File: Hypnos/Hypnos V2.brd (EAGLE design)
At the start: 25.5 x 51 mm, 25 parts

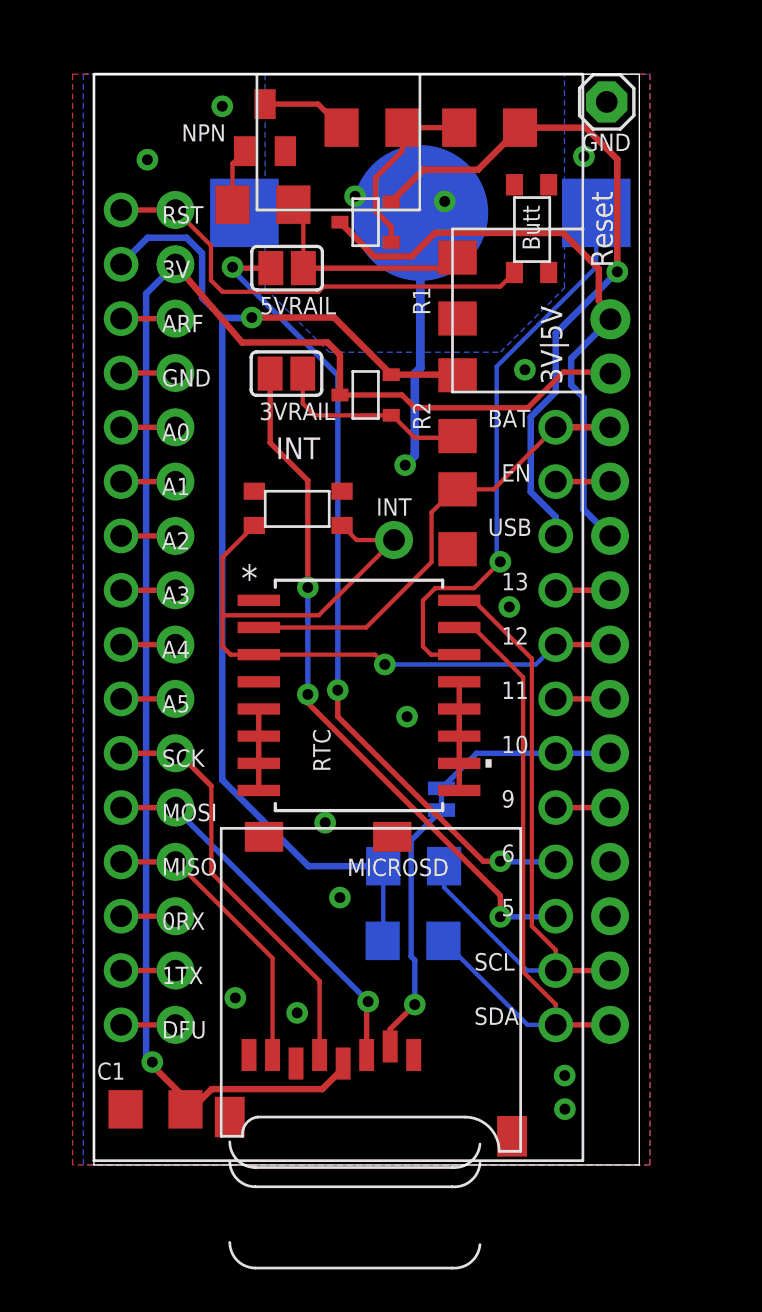
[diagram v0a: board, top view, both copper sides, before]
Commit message: Testing for Version V2
Update from Version 1:
* 2 LEDs with current limiting resistors
* RTC is now powered from 3V3 instead of Vbat (using power from Vbat turns on Feather Battery Charger LED)
* Pull up resistor for SD chip select just like adalogger
* Rounded PCB corner
* Move the reset button to the middle of the board - mechanically more stable
* Add solder jumper for RTC-INT, normally connected

These LED has very high efficiency and only draw around 2mA instead of 20mA
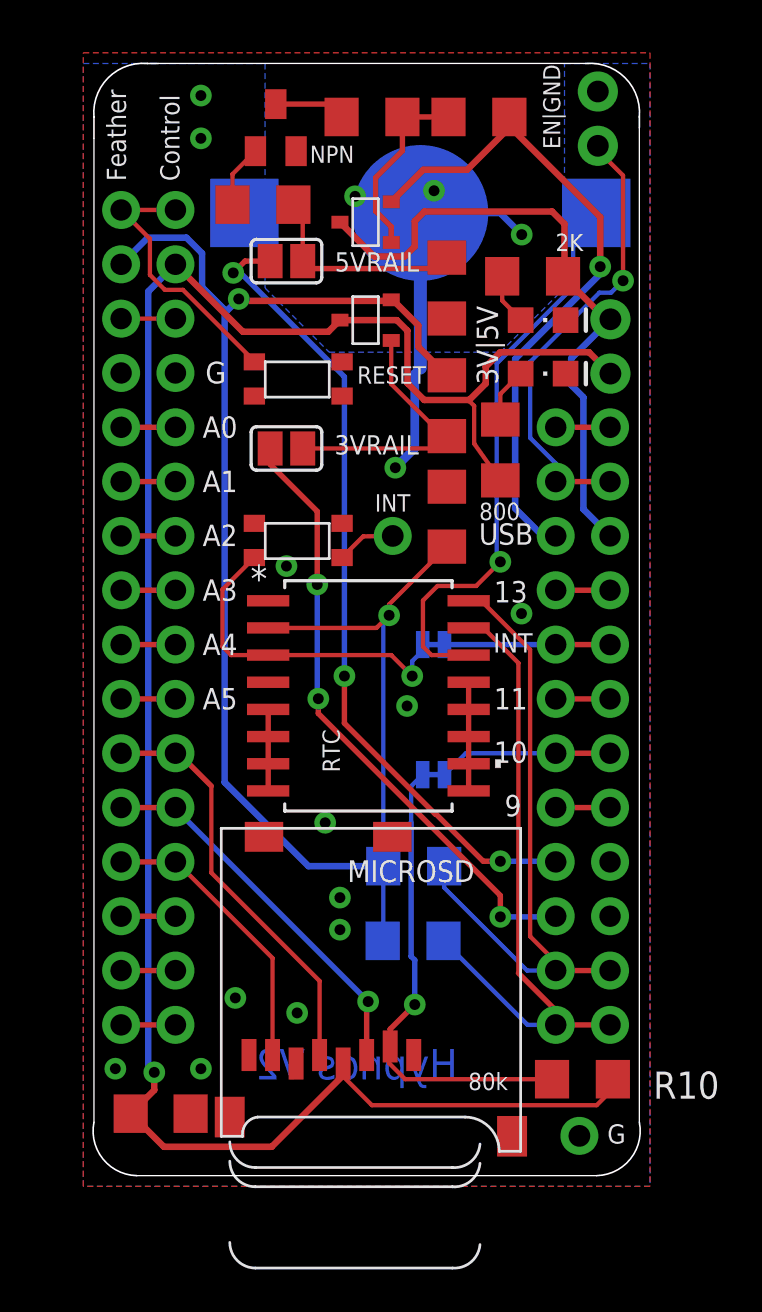
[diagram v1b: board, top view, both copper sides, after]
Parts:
- removed FEATHER: BLUEFRUIT_M0, bluefruit_m0:BLUEFRUIT_MO
- removed GND: (no value), adafruitmodified:1X01
- added EN|GND: (no value), SparkFun-Connectors:1X02_NO_SILK
- added JP1: (no value), adafruit:1X01-CLEANBIG
- added LED1, LED2: RED, adafruit:CHIPLED_0805
- added MS2: FEATHERWING, adafruit:FEATHERWING
- added R10: 80k, adafruit:R1206
- added R8: 2k, adafruit:R1206
- added R9: 820, adafruit:R1206
- added RTC_INT: (no value), SparkFun-Jumpers:SMT-JUMPER_2_NC_TRACE_SILK
- moved U$1 12.9 mm to (8.50, 38.5), turned to 0 degrees
- moved 3VRAIL 3.50 mm to (10.0, 34.5)
- moved PMOS2 3.50 mm to (13.7, 40.5)
- moved U$2 1.50 mm to (8.50, 31.0)
- moved CS 1.21 mm to (16.9, 19.2), turned to 0 degrees
- moved R4 0.71 mm to (19.0, 50.0)
- moved C3 0.51 mm to (17.5, 31.3), turned to 90 degrees
- moved NPN 0.50 mm to (9.50, 49.5)
- moved R1 0.50 mm to (17.5, 42.0)
- moved R2 0.50 mm to (17.5, 36.5)
- moved R5 0.50 mm to (14.0, 50.0)
- moved RTC 0.44 mm to (13.8, 22.9)
- moved 5VRAIL 0.33 mm to (10.0, 43.3)
- moved C1 0.31 mm to (4.12, 3.40), turned to 0 degrees
- moved INT 0.20 mm to (15.0, 30.4)
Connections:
- new net N$12: LED1.A, R8.1
- new net N$13: LED2.A, R9.1
- new net N$14: MS1.24, MS2.24, RTC_INT.1
- net +3V3: now also C3.1, MS2.2, RTC.2; no longer FEATHER.3V
- net 0RX: now also MS2.14; no longer FEATHER.0RX
- net 11: now also MS2.23; no longer FEATHER.11
- net 13: now also MS2.25; no longer FEATHER.13
- net 1TX: now also MS2.15; no longer FEATHER.1TX
- net 3VRAIL: now also R10.1, R9.2
- net 5VRAIL: now also R8.2
- net 5VUSB: now also MS2.26; no longer FEATHER.USB
- net 9: now also MS2.21; no longer FEATHER.9
- net A0: now also MS2.5; no longer FEATHER.A0
- net A1: now also MS2.6; no longer FEATHER.A1
- net A2: now also MS2.7; no longer FEATHER.A2
- net A3: now also MS2.8; no longer FEATHER.A3
- net A4: now also MS2.9; no longer FEATHER.A4
- net A5: now also MS2.10; no longer FEATHER.A5
- net ARF: now also MS2.3; no longer FEATHER.ARF
- net CLK: now also MS2.11; no longer FEATHER.SCK
- net CS: now also R10.2
- net DFU: now also MS2.16; no longer FEATHER.DFU
- net DI: now also MS2.12; no longer FEATHER.MOSI
- net DO: now also MS2.13; no longer FEATHER.MISO
- net EN: now also EN|GND.1, MS2.27; no longer FEATHER.EN
- net GND: now also EN|GND.2, JP1.1, LED1.C, LED2.C, MS2.4; no longer FEATHER.GND, GND.1
- net N$1: now also MS2.20; no longer FEATHER.6
- net N$11: now also MS2.22; no longer FEATHER.10
- net N$3: now also MS2.19; no longer FEATHER.5
- net RESET: now also MS2.1; no longer FEATHER.RST
- net RTC_INT: now also RTC_INT.2; no longer FEATHER.12, MS1.24
- net SCL: now also MS2.18; no longer FEATHER.SCL
- net SDA: now also MS2.17; no longer FEATHER.SDA
- net VBATT: now also MS2.28; no longer C3.1, FEATHER.BAT, RTC.2
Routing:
- net 3VRAIL: track 74.4 -> 98.9 mm
- net +3V3: track 54.4 -> 77.2 mm, vias 1 -> 2
- net VBATT: track 21.7 -> 2.54 mm
- net EN: track 2.54 -> 21.3 mm, vias 0 -> 1
- net RTC_INT: track 37.3 -> 18.7 mm
- net CS: track 12.2 -> 22.2 mm
- net RESET: track 21.3 -> 12.7 mm
- net N$14: track 0.00 -> 7.74 mm
- net GND: track 23.5 -> 31.1 mm, vias 15 -> 16
- net N$3: track 32.5 -> 29.0 mm
- net N$5: track 9.33 -> 12.6 mm
- net N$13: track 0.00 -> 2.54 mm
- net N$12: track 0.00 -> 2.43 mm
- net 5VRAIL: track 28.1 -> 30.1 mm
- net 5VUSB: track 32.4 -> 31.6 mm
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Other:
- board size 25.5 x 51 mm -> 25.6 x 52 mm
- board text added: "10K"
- board text added: "2K"
- board text added: "3V"
- board text added: "5V"
- board text added: "800"
- board text added: "80k"
- board text added: "Bao Nguyen"
- board text added: "Control"
- board text added: "Feather"
- board text added: "G"
- board text added: "Hypnos V2"
- board text added: "RESET"
- board text added: "RTC"
- board text removed: "12"
- board text removed: "3V Rail"
- board text removed: "5V Rail"
- board text removed: "Butt"
- board text removed: "Power RTC 3.3 V3"
- board text removed: "Reset"

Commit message: Schematic Change for Hypnos V2
Update Hypnos V2
* Change from BJT to Logic MOSFET. Using BJT require current limiting resistor and also involve more calculation.
* Remove R5 to simplify the circuit
* Increase trace width for all power rail
* Change resistors footprint to get more space and better indication for solder orientation

Update eDNA.lbr
* Add mosfet footprints
* Other footprints for power control related project

Update ReadMe
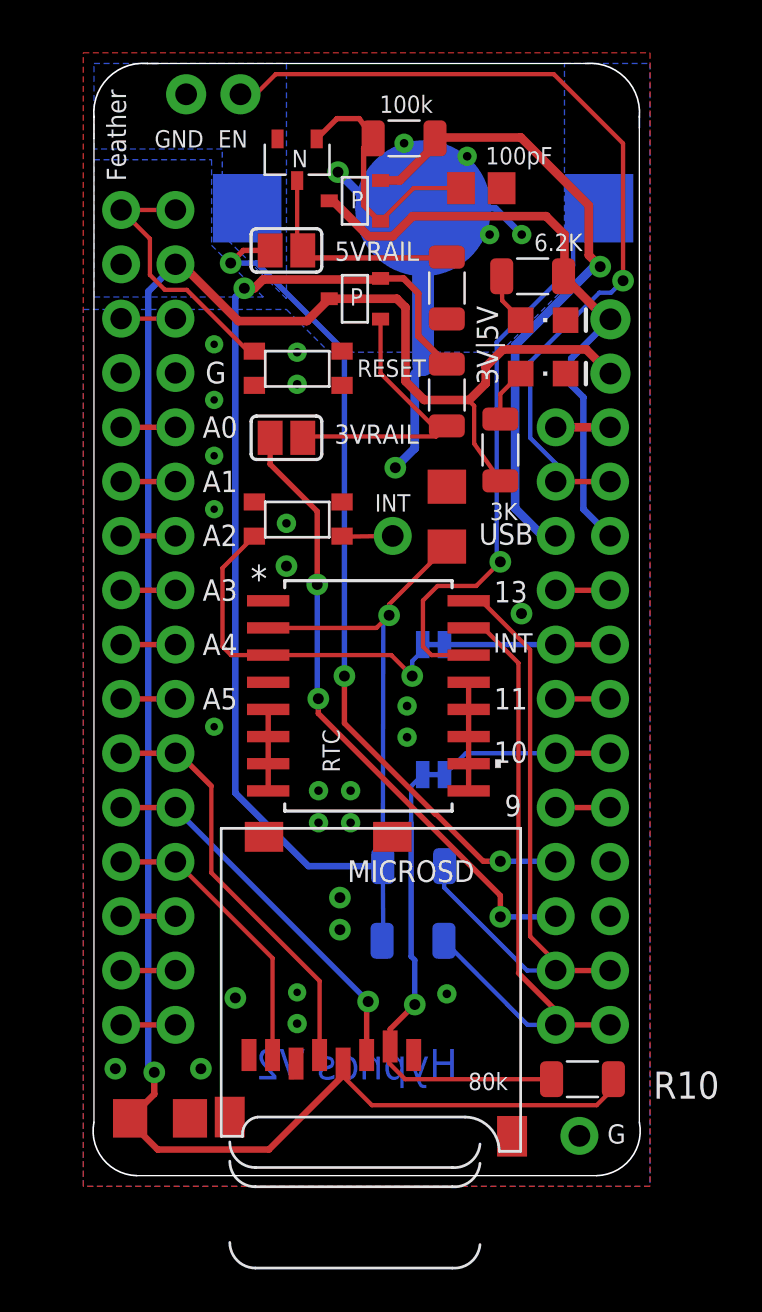
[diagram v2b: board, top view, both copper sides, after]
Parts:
- removed EN|GND: (no value), SparkFun-Connectors:1X02_NO_SILK
- removed NPN: SOT23, transistor:SOT23
- removed R3: 2M, adafruit:R1206
- removed R5: 20k, adafruit:R1206
- added C2: 100pF, resistor:C0805
- added GND|EN: (no value), SparkFun-Connectors:1X02_NO_SILK
- added U$3: NMOS, eDNA:SOT23-S
- C1, C3: device adafruit:C1206 -> resistor:C1206
- R1, R10, R2, R6, R7: device adafruit:R1206 -> Resistor_Capacitor:RES_1206
- R4: value 80k -> 100k; device adafruit:R1206 -> Resistor_Capacitor:RES_1206
- R8: value 2k -> 6.2k; device adafruit:R1206 -> Resistor_Capacitor:RES_1206
- R9: value 820 -> 3k; device adafruit:R1206 -> Resistor_Capacitor:RES_1206
- moved R4 3.64 mm to (15.5, 49.0)
- moved PMOS1 1.12 mm to (13.2, 46.1)
- moved PMOS2 1.12 mm to (13.2, 41.5)
- moved U$2 1.00 mm to (8.50, 32.0)
- moved 3VRAIL 0.50 mm to (10.0, 35.0)
- moved 5VRAIL 0.50 mm to (10.0, 43.8)
- moved R2 0.50 mm to (17.5, 37.0)
- moved U$1 0.50 mm to (8.50, 39.0)
- moved B1 0.26 mm to (16.4, 45.7)
- moved C1 0.22 mm to (4.09, 3.18)
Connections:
- removed net N$6: NPN.1, R3.2
- removed net N$9: NPN.3, R5.2
- net EN: now also GND|EN.1; no longer EN|GND.1
- net GND: now also C2.2, GND|EN.2, U$3.2; no longer EN|GND.2, NPN.2
- net N$10: now also C2.1, U$3.1; no longer R5.1
- net N$4: now also U$3.3; no longer R3.1
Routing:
- net EN: track 21.3 -> 40.6 mm
- net +3V3: track 77.2 -> 70.2 mm
- net N$10: track 8.85 -> 12.3 mm
- net N$9: track 3.33 -> 0.00 mm
- net N$6: track 2.94 -> 0.00 mm
- net 3VRAIL: track 98.9 -> 100.4 mm
- net N$5: track 12.6 -> 13.8 mm
- net N$1: track 37.9 -> 39.1 mm
- net 5VRAIL: track 30.1 -> 29.1 mm
- net 5VUSB: track 31.6 -> 30.7 mm
- net RTC_INT: track 18.7 -> 19.3 mm
- net N$3: track 29.0 -> 29.5 mm
- net GND: track 31.1 -> 31.4 mm, vias 16 -> 30
- added copper zone on layer 16, net +3V3
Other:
- board text added: "100k"
- board text added: "100pF"
- board text added: "3K"
- board text added: "6.2K"
- board text added: "N"
- board text added: "P"
- board text removed: "2K"
- board text removed: "800"

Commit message: N-Mos Bug FIx
Wrong footprint layout - Drain and Source was switched
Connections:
- net N$10: now also U$3.3; no longer U$3.1
- net N$4: now also U$3.1; no longer U$3.3
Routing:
- net N$4: track 10.3 -> 13.6 mm
- net GND: track 31.4 -> 34.3 mm
- net N$10: track 12.3 -> 13.3 mm
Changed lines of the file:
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@@
 <contactref element="GND|EN" pad="2"/>
 <wire x1="16.39" y1="45.73" x2="14.1" y2="45.73" width="0.2032" layer="16"/>
-<wire x1="14.1" y1="45.73" x2="12.41" y2="47.42" width="0.4064" layer="16"/>
+<wire x1="14.1" y1="45.73" x2="12.41" y2="47.42" width="0.508" layer="16"/>
 <contactref element="U$3" pad="2"/>
 <polygon width="0.254" layer="16">
@@
 <via x="10.5" y="9.07" extent="1-16" drill="0.35"/>
 <via x="18.45" y="48.16" extent="1-16" drill="0.4"/>
+<wire x1="12.41" y1="47.42" x2="12.08" y2="47.42" width="0.508" layer="16"/>
+<wire x1="12.41" y1="47.42" x2="11.58" y2="47.42" width="0.508" layer="16"/>
+<wire x1="11.58" y1="47.42" x2="11" y2="48" width="0.508" layer="16"/>
+<wire x1="11" y1="48" x2="10" y2="48" width="0.508" layer="16"/>
 <wire x1="20.06" y1="46.67" x2="19.5" y2="44.5" width="0" layer="19" extent="1-1"/>
 </signal>
@@
 <contactref element="R4" pad="2"/>
 <contactref element="PMOS1" pad="G"/>
-<contactref element="U$3" pad="1"/>
+<contactref element="U$3" pad="3"/>
 <wire x1="14.4" y1="45.13" x2="14.343025" y2="45.13" width="0.254" layer="1"/>
 <wire x1="14.343025" y1="45.13" x2="13.6082" y2="45.864825" width="0.254" layer="1"/>
-<wire x1="13.40486875" y1="49.922" x2="14.055" y2="49" width="0.254" layer="1"/>
-<wire x1="11.415" y1="48.9745" x2="12.3625" y2="49.922" width="0.254" layer="1"/>
-<wire x1="12.3625" y1="49.922" x2="13.40486875" y2="49.922" width="0.254" layer="1"/>
+<wire x1="14.055" y1="49" x2="13.977" y2="48.922" width="0.254" layer="1"/>
 <wire x1="14.055" y1="49" x2="13.6082" y2="48.5532" width="0.254" layer="1"/>
 <wire x1="13.6082" y1="48.5532" x2="13.6082" y2="45.864825" width="0.254" layer="1"/>
@@
 <wire x1="14.4" y1="45.13" x2="15.94" y2="46.67" width="0.2032" layer="1"/>
 <wire x1="15.94" y1="46.67" x2="18.16" y2="46.67" width="0.2032" layer="1"/>
+<wire x1="10.5" y1="47.0255" x2="10.657625" y2="47.0255" width="0.254" layer="1"/>
+<wire x1="12.632125" y1="49" x2="14.055" y2="49" width="0.254" layer="1"/>
+<wire x1="10.657625" y1="47.0255" x2="12.632125" y2="49" width="0.254" layer="1"/>
 </signal>
 <signal name="N$5">
@@
 <wire x1="17.466503125" y1="43.41" x2="11.112" y2="43.41" width="0.254" layer="1"/>
 <wire x1="11.112" y1="43.41" x2="10.762" y2="43.76" width="0.254" layer="1"/>
-<contactref element="U$3" pad="3"/>
+<contactref element="U$3" pad="1"/>
 <wire x1="10.762" y1="43.76" x2="10.5" y2="44.022" width="0.2032" layer="1"/>
-<wire x1="10.5" y1="44.022" x2="10.5" y2="47.0255" width="0.2032" layer="1"/>
+<wire x1="9.8852" y1="46.448675" x2="9.8852" y2="47.602325" width="0.254" layer="1"/>
+<wire x1="10.762" y1="43.76" x2="10.762" y2="45.571875" width="0.254" layer="1"/>
+<wire x1="10.762" y1="45.571875" x2="9.8852" y2="46.448675" width="0.254" layer="1"/>
+<wire x1="11.257375" y1="48.9745" x2="11.415" y2="48.9745" width="0.254" layer="1"/>
+<wire x1="11.257375" y1="48.9745" x2="9.8852" y2="47.602325" width="0.254" layer="1"/>
 </signal>
 <signal name="N$11">

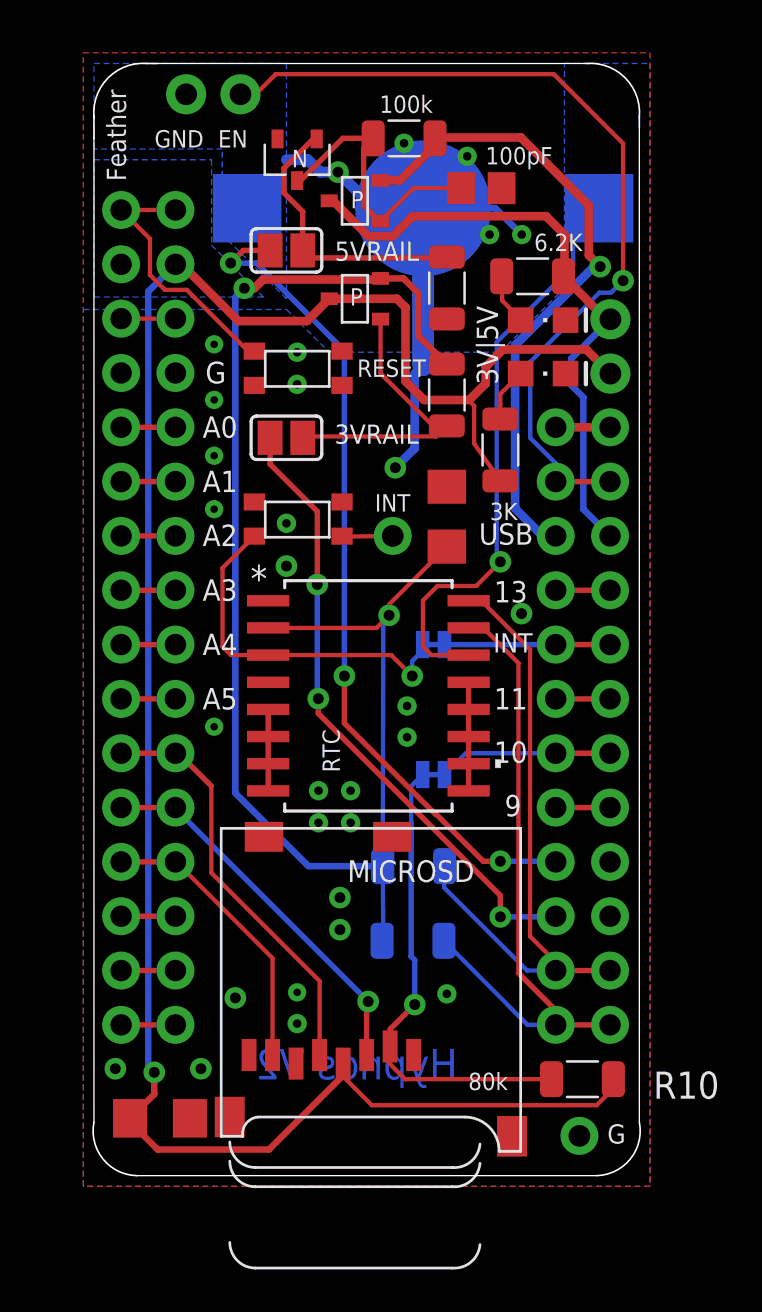
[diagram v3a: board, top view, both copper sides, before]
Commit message: Added Diode
Hardware fix for uSD card current leak. Added diode with low current leakage to prevent current from SPI pins going back to 3VRAIL.
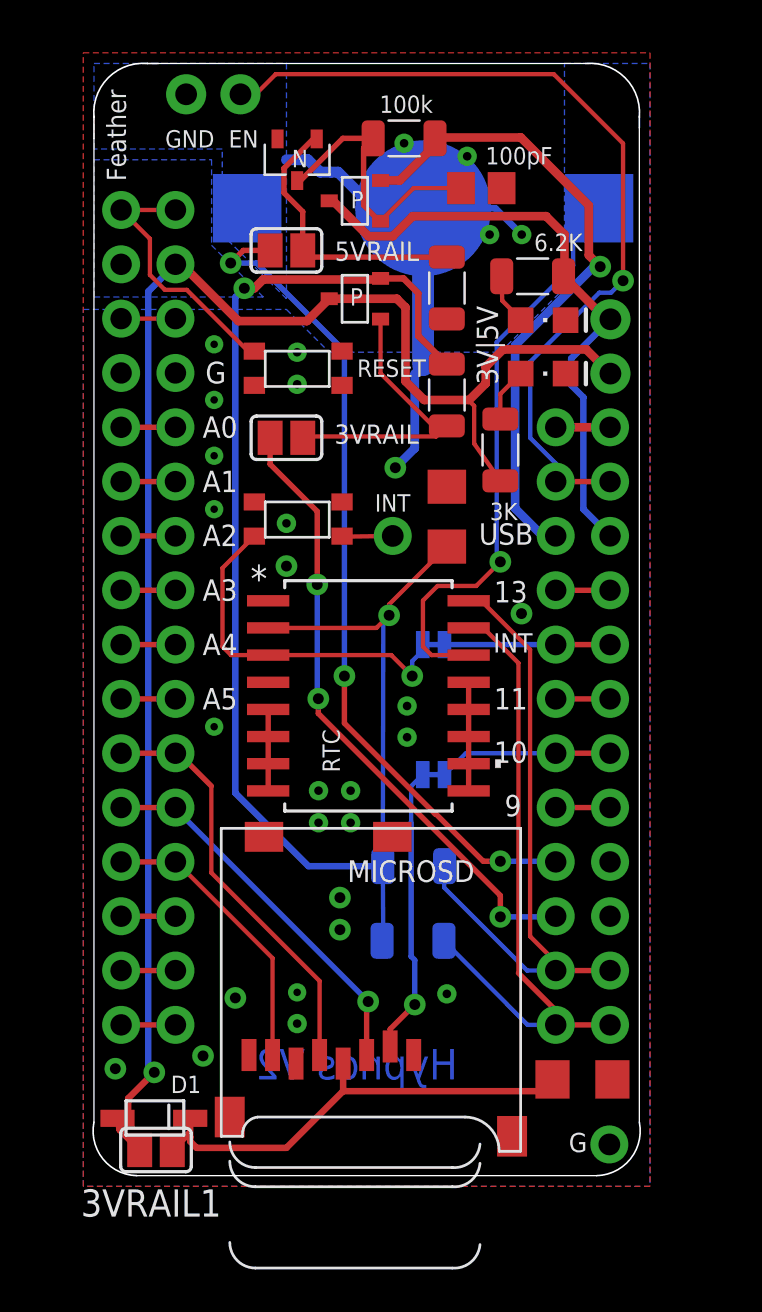
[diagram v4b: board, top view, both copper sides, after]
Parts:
- removed R10: 80k, Resistor_Capacitor:RES_1206
- added 3VRAIL1: (no value), jumper:SJ
- added D1: (no value), semicon-smd-ipc:SOD123
- moved C1 19.8 mm to (23.8, 5.00)
- moved JP1 1.46 mm to (25.1, 1.96)
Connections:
- new net VDD: 3VRAIL1.1, C1.1, D1.1, MICROSD.4
- net 3VRAIL: now also 3VRAIL1.2, D1.2; no longer C1.1, MICROSD.4, R10.1
- net CS: no longer R10.2
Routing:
- net 3VRAIL: track 100.4 -> 75.3 mm
- net VDD: track 0.00 -> 22.0 mm
- net CS: track 22.2 -> 13.5 mm
- net GND: track 34.3 -> 34.0 mm, vias 30 -> 29
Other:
- board text removed: "80k"
